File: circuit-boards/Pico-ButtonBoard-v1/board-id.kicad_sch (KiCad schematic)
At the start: 7 parts, among them J24 ID

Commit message: Update footprints
Signed-off-by: Scott Berman <sgberman1@gmail.com>
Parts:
- J501: renamed from J24; footprint (none) -> Pico-ButtonBoard:Molex-70555-0038
- R503: renamed from R68; DIST (none) -> Digikey; DIST P/N (none) -> 541-10.0KCCT-ND; MFG (none) -> Vishay Dale; MFG P/N (none) -> CRCW080510K0FKEA
- R504: renamed from R70; DIST (none) -> Digikey; DIST P/N (none) -> 541-10.0KCCT-ND; MFG (none) -> Vishay Dale; MFG P/N (none) -> CRCW080510K0FKEA
- renumbered C38 to C501, C39 to C502, R67 to R501, R69 to R502
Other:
- title: (none) -> Pico Button Board
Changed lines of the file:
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@@
 	(paper "B")
 	(title_block
+		(title "Pico Button Board")
 		(date "2025-12-25")
+		(rev "1")
 	)
 	(text "GND"
@@
 		(on_board yes)
 		(dnp no)
-		(property "Reference" "R68"
+		(property "Reference" "R503"
 			(at 216.408 129.54 90)
 			(effects
@@
 			)
 		)
-		(property "MFG" ""
+		(property "MFG" "Vishay Dale"
 			(at 220.98 128.27 0)
 			(effects
@@
 			)
 		)
-		(property "MFG P/N" ""
+		(property "MFG P/N" "CRCW080510K0FKEA"
 			(at 220.98 128.27 0)
 			(effects
@@
 			)
 		)
-		(property "DIST" ""
+		(property "DIST" "Digikey"
 			(at 220.98 128.27 0)
 			(effects
@@
 			)
 		)
-		(property "DIST P/N" ""
+		(property "DIST P/N" "541-10.0KCCT-ND"
 			(at 220.98 128.27 0)
+			(effects
+				(font
+					(size 1.27 1.27)
+				)
+				(hide yes)
+			)
+		)
+		(property "Sim.Device" ""
+			(at 220.98 128.27 90)
+			(effects
+				(font
+					(size 1.27 1.27)
+				)
+				(hide yes)
+			)
+		)
+		(property "Sim.Type" ""
+			(at 220.98 128.27 90)
 			(effects
 				(font
@@
 			(project "Pico-ButtonBoard-v1"
 				(path "/644201a9-3a2f-4df3-9c93-2ae55394df4b/4e285169-a0a4-4eb6-9253-4dccf3a51578"
-					(reference "R68")
+					(reference "R503")
 					(unit 1)
 				)
@@
 		(on_board yes)
 		(dnp no)
-		(property "Reference" "C39"
+		(property "Reference" "C502"
 			(at 201.93 144.78 90)
 			(effects
@@
 		(property "MFG P/N" "311-1141-1-ND"
 			(at 200.66 146.05 0)
+			(effects
+				(font
+					(size 1.27 1.27)
+				)
+				(hide yes)
+			)
+		)
+		(property "Sim.Device" ""
+			(at 200.66 146.05 90)
+			(effects
+				(font
+					(size 1.27 1.27)
+				)
+				(hide yes)
+			)
+		)
+		(property "Sim.Type" ""
+			(at 200.66 146.05 90)
 			(effects
 				(font
@@
 			(project "Pico-ButtonBoard-v1"
 				(path "/644201a9-3a2f-4df3-9c93-2ae55394df4b/4e285169-a0a4-4eb6-9253-4dccf3a51578"
-					(reference "C39")
+					(reference "C502")
 					(unit 1)
 				)
@@
 		(on_board yes)
 		(dnp no)
-		(property "Reference" "#PWR0103"
+		(property "Reference" "#PWR0504"
 			(at 189.23 162.56 0)
 			(effects
@@
 			(project "Pico-ButtonBoard-v1"
 				(path "/644201a9-3a2f-4df3-9c93-2ae55394df4b/4e285169-a0a4-4eb6-9253-4dccf3a51578"
-					(reference "#PWR0103")
+					(reference "#PWR0504")
 					(unit 1)
 				)
@@
 		(on_board yes)
 		(dnp no)
-		(property "Reference" "#PWR0107"
+		(property "Reference" "#PWR0501"
 			(at 144.78 144.78 0)
 			(effects
@@
 			(project "Pico-ButtonBoard-v1"
 				(path "/644201a9-3a2f-4df3-9c93-2ae55394df4b/4e285169-a0a4-4eb6-9253-4dccf3a51578"
-					(reference "#PWR0107")
+					(reference "#PWR0501")
 					(unit 1)
 				)
@@
 		(on_board yes)
 		(dnp no)
-		(property "Reference" "#PWR0104"
+		(property "Reference" "#PWR0502"
 			(at 173.99 114.3 0)
 			(effects
@@
 			(project "Pico-ButtonBoard-v1"
 				(path "/644201a9-3a2f-4df3-9c93-2ae55394df4b/4e285169-a0a4-4eb6-9253-4dccf3a51578"
-					(reference "#PWR0104")
+					(reference "#PWR0502")
 					(unit 1)
 				)
@@
 		(on_board yes)
 		(dnp no)
-		(property "Reference" "#PWR0106"
+		(property "Reference" "#PWR0505"
 			(at 200.66 162.56 0)
 			(effects
@@
 			(project "Pico-ButtonBoard-v1"
 				(path "/644201a9-3a2f-4df3-9c93-2ae55394df4b/4e285169-a0a4-4eb6-9253-4dccf3a51578"
-					(reference "#PWR0106")
+					(reference "#PWR0505")
 					(unit 1)
 				)
@@
 		(on_board yes)
 		(dnp no)
-		(property "Reference" "C38"
+		(property "Reference" "C501"
 			(at 190.5 144.78 90)
 			(effects
@@
 		(property "MFG P/N" "311-1141-1-ND"
 			(at 189.23 146.05 0)
+			(effects
+				(font
+					(size 1.27 1.27)
+				)
+				(hide yes)
+			)
+		)
+		(property "Sim.Device" ""
+			(at 189.23 146.05 90)
+			(effects
+				(font
+					(size 1.27 1.27)
+				)
+				(hide yes)
+			)
+		)
+		(property "Sim.Type" ""
+			(at 189.23 146.05 90)
 			(effects
 				(font
@@
 			(project "Pico-ButtonBoard-v1"
 				(path "/644201a9-3a2f-4df3-9c93-2ae55394df4b/4e285169-a0a4-4eb6-9253-4dccf3a51578"
-					(reference "C38")
+					(reference "C501")
 					(unit 1)
 				)
@@
 		(on_board yes)
 		(dnp no)
-		(property "Reference" "R69"
+		(property "Reference" "R502"
 			(at 183.896 118.872 90)
 			(effects
@@
 		(property "DIST P/N" "311-1.50KCRCT-ND"
 			(at 182.88 116.84 0)
+			(effects
+				(font
+					(size 1.27 1.27)
+				)
+				(hide yes)
+			)
+		)
+		(property "Sim.Device" ""
+			(at 182.88 116.84 90)
+			(effects
+				(font
+					(size 1.27 1.27)
+				)
+				(hide yes)
+			)
+		)
+		(property "Sim.Type" ""
+			(at 182.88 116.84 90)
 			(effects
 				(font
@@
 			(project "Pico-ButtonBoard-v1"
 				(path "/644201a9-3a2f-4df3-9c93-2ae55394df4b/4e285169-a0a4-4eb6-9253-4dccf3a51578"
-					(reference "R69")
+					(reference "R502")
 					(unit 1)
 				)
@@
 		(on_board yes)
 		(dnp no)
-		(property "Reference" "#PWR0105"
+		(property "Reference" "#PWR0503"
 			(at 182.88 114.3 0)
 			(effects
@@
 			(project "Pico-ButtonBoard-v1"
 				(path "/644201a9-3a2f-4df3-9c93-2ae55394df4b/4e285169-a0a4-4eb6-9253-4dccf3a51578"
-					(reference "#PWR0105")
+					(reference "#PWR0503")
 					(unit 1)
 				)
@@
 		(on_board yes)
 		(dnp no)
-		(property "Reference" "R70"
+		(property "Reference" "R504"
 			(at 216.408 132.334 90)
 			(effects
@@
 			)
 		)
-		(property "MFG" ""
+		(property "MFG" "Vishay Dale"
 			(at 220.98 133.35 0)
 			(effects
@@
 			)
 		)
-		(property "MFG P/N" ""
+		(property "MFG P/N" "CRCW080510K0FKEA"
 			(at 220.98 133.35 0)
 			(effects
@@
 			)
 		)
-		(property "DIST" ""
+		(property "DIST" "Digikey"
 			(at 220.98 133.35 0)
 			(effects
@@
 			)
 		)
-		(property "DIST P/N" ""
+		(property "DIST P/N" "541-10.0KCCT-ND"
 			(at 220.98 133.35 0)
+			(effects
+				(font
+					(size 1.27 1.27)
+				)
+				(hide yes)
+			)
+		)
+		(property "Sim.Device" ""
+			(at 220.98 133.35 90)
+			(effects
+				(font
+					(size 1.27 1.27)
+				)
+				(hide yes)
+			)
+		)
+		(property "Sim.Type" ""
+			(at 220.98 133.35 90)
 			(effects
 				(font
@@
 			(project "Pico-ButtonBoard-v1"
 				(path "/644201a9-3a2f-4df3-9c93-2ae55394df4b/4e285169-a0a4-4eb6-9253-4dccf3a51578"
-					(reference "R70")
+					(reference "R504")
 					(unit 1)
 				)
@@
 		(on_board yes)
 		(dnp no)
-		(property "Reference" "R67"
+		(property "Reference" "R501"
 			(at 175.006 118.872 90)
 			(effects
@@
 		(property "DIST P/N" "311-1.50KCRCT-ND"
 			(at 173.99 116.84 0)
+			(effects
+				(font
+					(size 1.27 1.27)
+				)
+				(hide yes)
+			)
+		)
+		(property "Sim.Device" ""
+			(at 173.99 116.84 90)
+			(effects
+				(font
+					(size 1.27 1.27)
+				)
+				(hide yes)
+			)
+		)
+		(property "Sim.Type" ""
+			(at 173.99 116.84 90)
 			(effects
 				(font
@@
 			(project "Pico-ButtonBoard-v1"
 				(path "/644201a9-3a2f-4df3-9c93-2ae55394df4b/4e285169-a0a4-4eb6-9253-4dccf3a51578"
-					(reference "R67")
+					(reference "R501")
 					(unit 1)
 				)
@@
 		(on_board yes)
 		(dnp no)
-		(property "Reference" "J24"
+		(property "Reference" "J501"
 			(at 137.16 121.412 0)
 			(effects
@@
 			)
 		)
-		(property "Footprint" ""
+		(property "Footprint" "Pico-ButtonBoard:Molex-70555-0038"
 			(at 137.16 128.27 0)
 			(effects
@@
 			)
 		)
-		(property "Datasheet" "~"
+		(property "Datasheet" "Components/Molex-70555-0001.pdf"
 			(at 137.16 128.27 0)
 			(effects
@@
 		)
 		(property "DIST P/N" "538-70555-0038"
+			(at 137.16 128.27 0)
+			(effects
+				(font
+					(size 1.27 1.27)
+				)
+				(hide yes)
+			)
+		)
+		(property "Sim.Device" ""
+			(at 137.16 128.27 0)
+			(effects
+				(font
+					(size 1.27 1.27)
+				)
+				(hide yes)
+			)
+		)
+		(property "Sim.Type" ""
 			(at 137.16 128.27 0)
 			(effects
@@
 			(project "Pico-ButtonBoard-v1"
 				(path "/644201a9-3a2f-4df3-9c93-2ae55394df4b/4e285169-a0a4-4eb6-9253-4dccf3a51578"
-					(reference "J24")
+					(reference "J501")
 					(unit 1)
 				)

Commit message: Pico Button Board initial placement
Signed-off-by: Scott Berman <sgberman1@gmail.com>
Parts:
- C501, C502: LCSC Part # C519981 -> (none)
- J501: footprint Pico-ButtonBoard:Molex-70555-0038 -> Pico-ButtonBoard:Molex-70543-0003; DIST P/N 538-70555-0038 -> WM4826-ND; MFG P/N 70555-0038 -> 0705430038
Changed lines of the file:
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@@
-			)
-		)
-		(property "Sim.Device" ""
-			(at 220.98 128.27 90)
-			(effects
-				(font
-					(size 1.27 1.27)
-				)
-				(hide yes)
-			)
-		)
-		(property "Sim.Type" ""
-			(at 220.98 128.27 90)
-			(effects
-				(font
-					(size 1.27 1.27)
-				)
-				(hide yes)
 			)
 		)
@@
 			)
 		)
-		(property "JLCPCB" ""
-			(at 200.66 146.05 0)
-			(effects
-				(font
-					(size 1.27 1.27)
-				)
-				(hide yes)
-			)
-		)
-		(property "LCSC Part #" "C519981"
-			(at 200.66 146.05 0)
-			(effects
-				(font
-					(size 1.27 1.27)
-				)
-				(hide yes)
-			)
-		)
 		(property "DIST" "Digikey"
 			(at 200.66 146.05 0)
@@
 		(property "MFG P/N" "311-1141-1-ND"
 			(at 200.66 146.05 0)
-			(effects
-				(font
-					(size 1.27 1.27)
-				)
-				(hide yes)
-			)
-		)
-		(property "Sim.Device" ""
-			(at 200.66 146.05 90)
-			(effects
-				(font
-					(size 1.27 1.27)
-				)
-				(hide yes)
-			)
-		)
-		(property "Sim.Type" ""
-			(at 200.66 146.05 90)
 			(effects
 				(font
@@
 			)
 		)
-		(property "JLCPCB" ""
-			(at 189.23 146.05 0)
-			(effects
-				(font
-					(size 1.27 1.27)
-				)
-				(hide yes)
-			)
-		)
-		(property "LCSC Part #" "C519981"
-			(at 189.23 146.05 0)
-			(effects
-				(font
-					(size 1.27 1.27)
-				)
-				(hide yes)
-			)
-		)
 		(property "DIST" "Digikey"
 			(at 189.23 146.05 0)
@@
 			)
 		)
-		(property "Sim.Device" ""
-			(at 189.23 146.05 90)
-			(effects
-				(font
-					(size 1.27 1.27)
-				)
-				(hide yes)
-			)
-		)
-		(property "Sim.Type" ""
-			(at 189.23 146.05 90)
-			(effects
-				(font
-					(size 1.27 1.27)
-				)
-				(hide yes)
-			)
-		)
 		(pin "2"
 		)
@@
 		(property "DIST P/N" "311-1.50KCRCT-ND"
 			(at 182.88 116.84 0)
-			(effects
-				(font
-					(size 1.27 1.27)
-				)
-				(hide yes)
-			)
-		)
-		(property "Sim.Device" ""
-			(at 182.88 116.84 90)
-			(effects
-				(font
-					(size 1.27 1.27)
-				)
-				(hide yes)
-			)
-		)
-		(property "Sim.Type" ""
-			(at 182.88 116.84 90)
 			(effects
 				(font
@@
 			)
 		)
-		(property "Sim.Device" ""
-			(at 220.98 133.35 90)
-			(effects
-				(font
-					(size 1.27 1.27)
-				)
-				(hide yes)
-			)
-		)
-		(property "Sim.Type" ""
-			(at 220.98 133.35 90)
-			(effects
-				(font
-					(size 1.27 1.27)
-				)
-				(hide yes)
-			)
-		)
 		(pin "1"
 		)
@@
 		(property "DIST P/N" "311-1.50KCRCT-ND"
 			(at 173.99 116.84 0)
-			(effects
-				(font
-					(size 1.27 1.27)
-				)
-				(hide yes)
-			)
-		)
-		(property "Sim.Device" ""
-			(at 173.99 116.84 90)
-			(effects
-				(font
-					(size 1.27 1.27)
-				)
-				(hide yes)
-			)
-		)
-		(property "Sim.Type" ""
-			(at 173.99 116.84 90)
 			(effects
 				(font
@@
 			)
 		)
-		(property "Footprint" "Pico-ButtonBoard:Molex-70555-0038"
+		(property "Footprint" "Pico-ButtonBoard:Molex-70543-0003"
 			(at 137.16 128.27 0)
 			(effects
@@
 			)
 		)
-		(property "Datasheet" "Components/Molex-70555-0001.pdf"
+		(property "Datasheet" "Components/Molex-705430001_sd.pdf"
 			(at 137.16 128.27 0)
 			(effects
@@
 		)
 		(property "MFG" "Molex"
-			(at 137.16 128.27 0)
-			(effects
-				(font
-					(size 1.27 1.27)
-				)
-				(hide yes)
-			)
-		)
-		(property "MFG P/N" "70555-0038"
-			(at 137.16 128.27 0)
-			(effects
-				(font
-					(size 1.27 1.27)
-				)
-				(hide yes)
+			(at 118.618 136.398 0)
+			(show_name yes)
+			(effects
+				(font
+					(size 1.27 1.27)
+				)
+				(justify right)
+			)
+		)
+		(property "MFG P/N" "0705430038"
+			(at 118.618 138.43 0)
+			(show_name yes)
+			(effects
+				(font
+					(size 1.27 1.27)
+				)
+				(justify right)
 			)
 		)
@@
 			)
 		)
-		(property "DIST P/N" "538-70555-0038"
+		(property "DIST P/N" "WM4826-ND"
 			(at 137.16 128.27 0)
 			(effects
-				(font
-					(size 1.27 1.27)
-				)
-				(hide yes)
-			)
-		)
-		(property "Sim.Device" ""
-			(at 137.16 128.27 0)
-			(effects
-				(font
-					(size 1.27 1.27)
-				)
-				(hide yes)
-			)
-		)
-		(property "Sim.Type" ""
-			(at 137.16 128.27 0)
-			(effects

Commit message: Pico Button Board initial pcb checkin
Signed-off-by: Scott Berman <sgberman1@gmail.com>
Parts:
- renumbered C502 to C31, C501 to C32, J501 to J12, R503 to R10, R501 to R11, R504 to R8, R502 to R9
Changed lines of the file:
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@@
 		(on_board yes)
 		(dnp no)
-		(property "Reference" "R503"
+		(property "Reference" "R10"
 			(at 216.408 129.54 90)
 			(effects
@@
 			(project "Pico-ButtonBoard-v1"
 				(path "/644201a9-3a2f-4df3-9c93-2ae55394df4b/4e285169-a0a4-4eb6-9253-4dccf3a51578"
-					(reference "R503")
+					(reference "R10")
 					(unit 1)
 				)
@@
 		(on_board yes)
 		(dnp no)
-		(property "Reference" "C502"
+		(property "Reference" "C31"
 			(at 201.93 144.78 90)
 			(effects
@@
 			(project "Pico-ButtonBoard-v1"
 				(path "/644201a9-3a2f-4df3-9c93-2ae55394df4b/4e285169-a0a4-4eb6-9253-4dccf3a51578"
-					(reference "C502")
+					(reference "C31")
 					(unit 1)
 				)
@@
 		(on_board yes)
 		(dnp no)
-		(property "Reference" "C501"
+		(property "Reference" "C32"
 			(at 190.5 144.78 90)
 			(effects
@@
 			(project "Pico-ButtonBoard-v1"
 				(path "/644201a9-3a2f-4df3-9c93-2ae55394df4b/4e285169-a0a4-4eb6-9253-4dccf3a51578"
-					(reference "C501")
+					(reference "C32")
 					(unit 1)
 				)
@@
 		(on_board yes)
 		(dnp no)
-		(property "Reference" "R502"
+		(property "Reference" "R9"
 			(at 183.896 118.872 90)
 			(effects
@@
 			(project "Pico-ButtonBoard-v1"
 				(path "/644201a9-3a2f-4df3-9c93-2ae55394df4b/4e285169-a0a4-4eb6-9253-4dccf3a51578"
-					(reference "R502")
+					(reference "R9")
 					(unit 1)
 				)
@@
 		(on_board yes)
 		(dnp no)
-		(property "Reference" "R504"
+		(property "Reference" "R8"
 			(at 216.408 132.334 90)
 			(effects
@@
 			(project "Pico-ButtonBoard-v1"
 				(path "/644201a9-3a2f-4df3-9c93-2ae55394df4b/4e285169-a0a4-4eb6-9253-4dccf3a51578"
-					(reference "R504")
+					(reference "R8")
 					(unit 1)
 				)
@@
 		(on_board yes)
 		(dnp no)
-		(property "Reference" "R501"
+		(property "Reference" "R11"
 			(at 175.006 118.872 90)
 			(effects
@@
 			(project "Pico-ButtonBoard-v1"
 				(path "/644201a9-3a2f-4df3-9c93-2ae55394df4b/4e285169-a0a4-4eb6-9253-4dccf3a51578"
-					(reference "R501")
+					(reference "R11")
 					(unit 1)
 				)
@@
 		(on_board yes)
 		(dnp no)
-		(property "Reference" "J501"
+		(property "Reference" "J12"
 			(at 137.16 121.412 0)
 			(effects
@@
 			(project "Pico-ButtonBoard-v1"
 				(path "/644201a9-3a2f-4df3-9c93-2ae55394df4b/4e285169-a0a4-4eb6-9253-4dccf3a51578"
-					(reference "J501")
-					(unit 1)
-				)
+					(reference "J12")
+					(unit 1)
+				)

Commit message: Changed button input circuit to use mux. Changed ADC3 to an external SPI ADC
Signed-off-by: Scott Berman <sgberman1@gmail.com>
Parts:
- renumbered C31 to C30, C32 to C31, J12 to J1

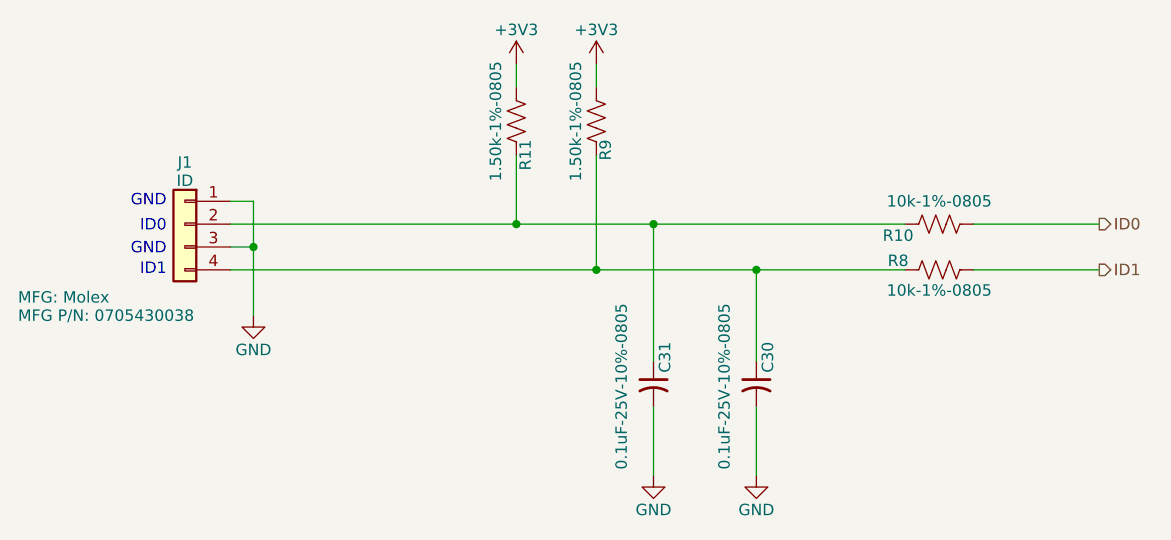
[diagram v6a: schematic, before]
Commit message: Change diodes to schottky. Change 5V setpoint to 5.18V
Signed-off-by: Scott Berman <sgberman1@gmail.com>
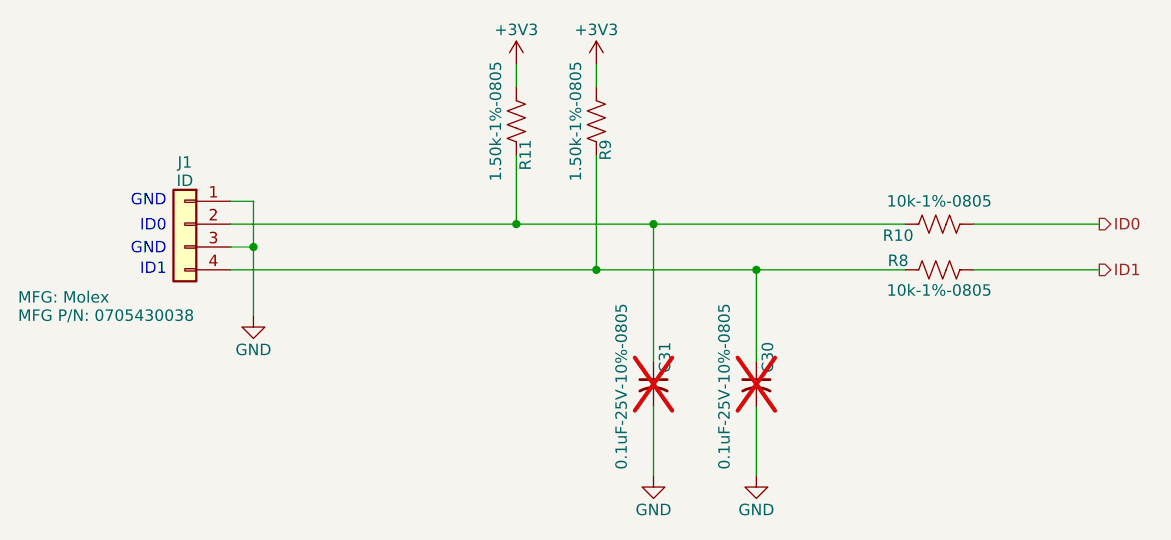
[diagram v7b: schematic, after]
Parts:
- C30, C31: now not fitted
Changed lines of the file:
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@@
 	(title_block
 		(title "Pico Button Board")
-		(date "2025-12-30")
+		(date "2025-12-31")
 		(rev "1")
 	)
@@
 		(in_bom yes)
 		(on_board yes)
-		(dnp no)
+		(dnp yes)
 		(property "Reference" "C30"
 			(at 201.93 144.78 90)
@@
 		(in_bom yes)
 		(on_board yes)
-		(dnp no)
+		(dnp yes)
 		(property "Reference" "C31"
 			(at 190.5 144.78 90)

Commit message: Added power indicator to button board
Signed-off-by: Scott Berman <sgberman1@gmail.com>
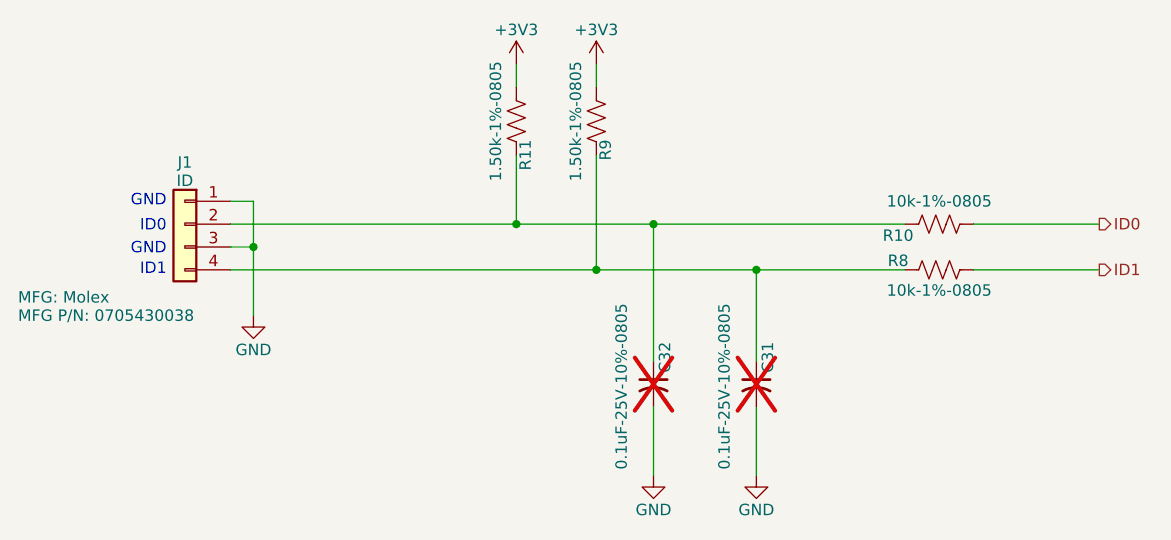
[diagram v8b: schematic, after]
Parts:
- renumbered C30 to C31, C31 to C32
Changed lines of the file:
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@@
 	(title_block
 		(title "Pico Button Board")
-		(date "2025-12-31")
+		(date "2026-01-20")
 		(rev "1")
 	)
@@
 		(on_board yes)
 		(dnp yes)
-		(property "Reference" "C30"
+		(property "Reference" "C31"
 			(at 201.93 144.78 90)
 			(effects
@@
 			(project "Pico-ButtonBoard-v1"
 				(path "/644201a9-3a2f-4df3-9c93-2ae55394df4b/4e285169-a0a4-4eb6-9253-4dccf3a51578"
-					(reference "C30")
+					(reference "C31")
 					(unit 1)
 				)
@@
 		(on_board yes)
 		(dnp yes)
-		(property "Reference" "C31"
+		(property "Reference" "C32"
 			(at 190.5 144.78 90)
 			(effects
@@
 			(project "Pico-ButtonBoard-v1"
 				(path "/644201a9-3a2f-4df3-9c93-2ae55394df4b/4e285169-a0a4-4eb6-9253-4dccf3a51578"
-					(reference "C31")
+					(reference "C32")
 					(unit 1)
 				)
